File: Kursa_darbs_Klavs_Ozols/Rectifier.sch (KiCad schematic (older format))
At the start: 75 parts, among them U10 TL074, U11 TL074, U12 TL074

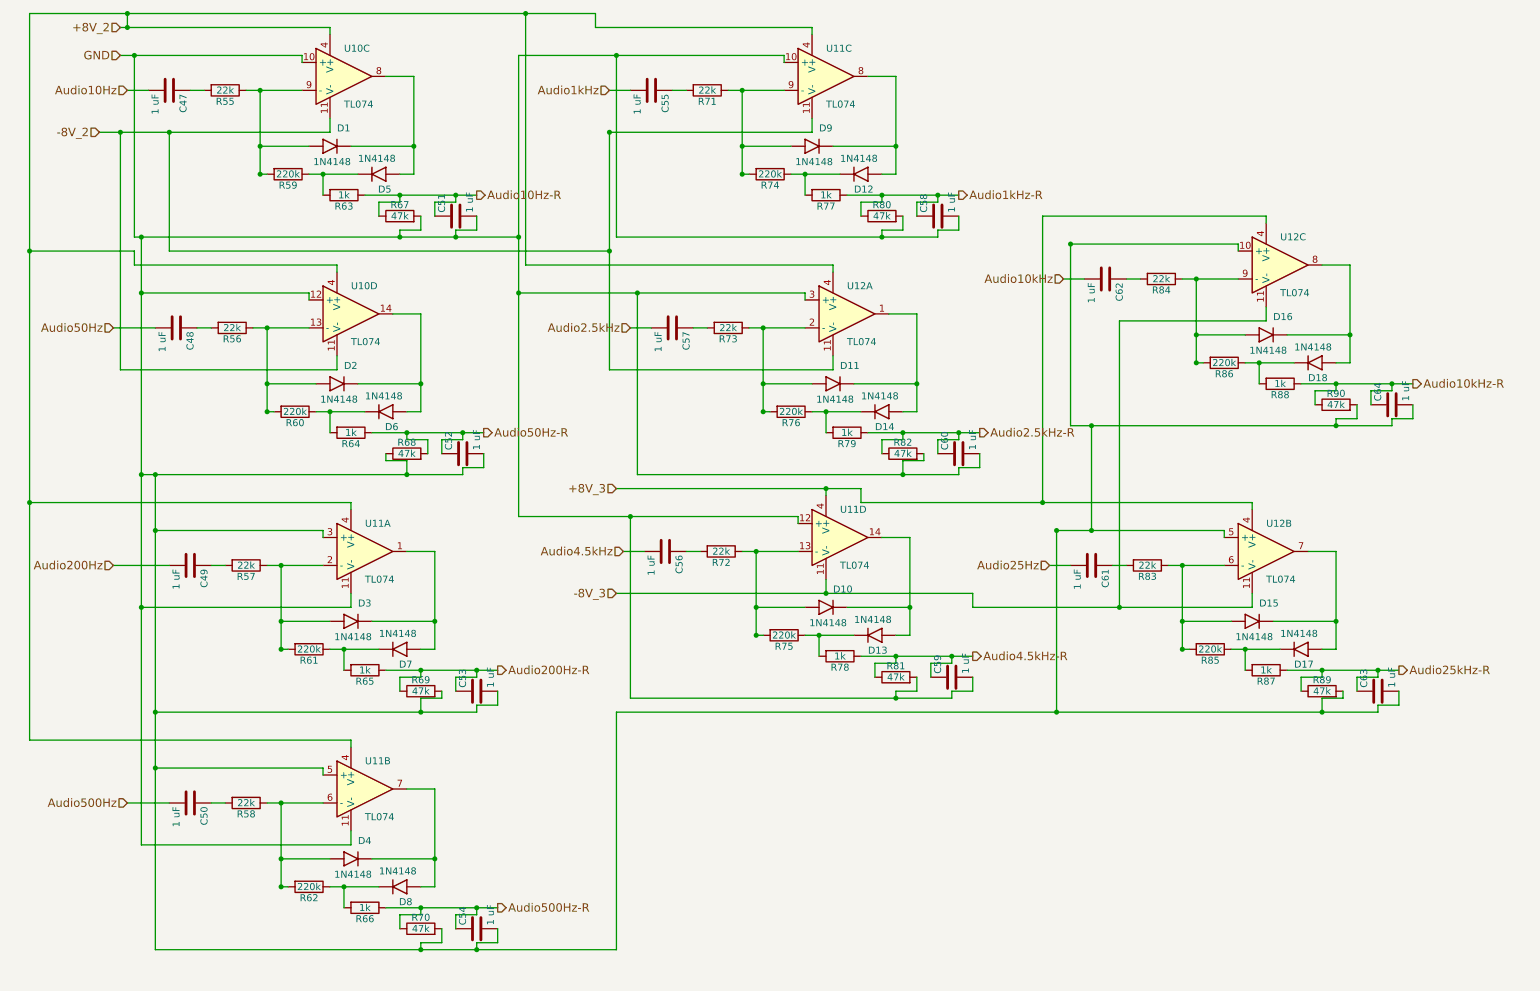
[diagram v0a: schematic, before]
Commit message: Kursa darba plates 4. iteraacija
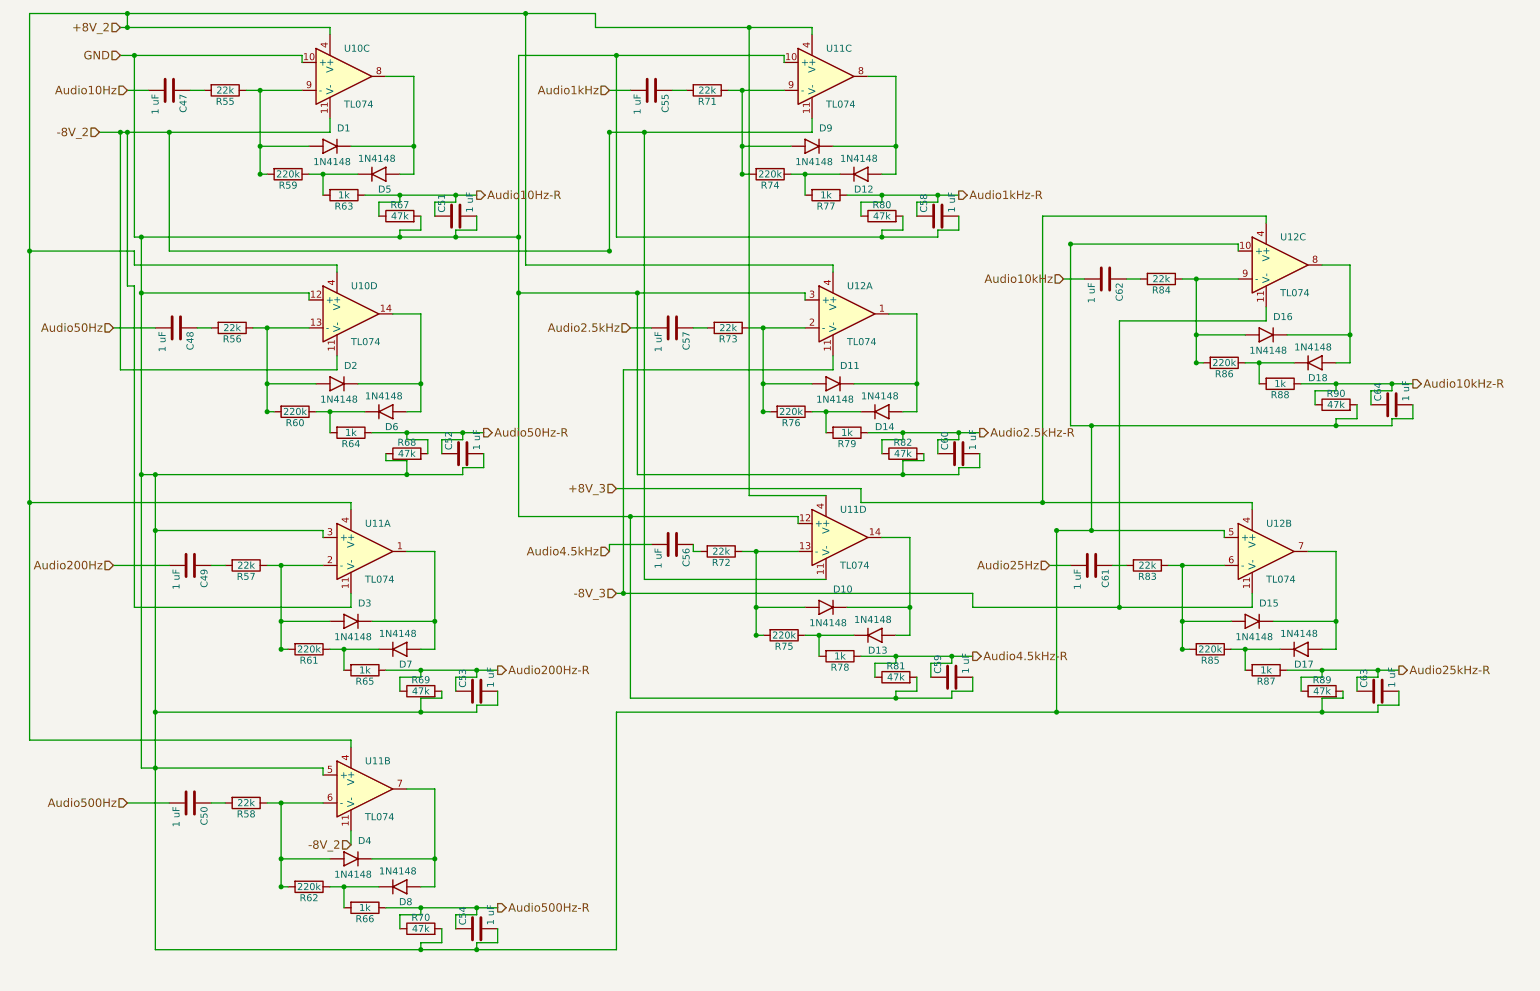
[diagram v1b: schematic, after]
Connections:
- net +8V_2: now also U11.4 (V+)
- net +8V_3: no longer U11.4 (V+)
- net -8V_2: now also U11.11 (V-), U11.11 (V-), U11.11 (V-); no longer U12.11 (V-)
- net -8V_3: now also U12.11 (V-); no longer U11.11 (V-)
- net GND: no longer U11.11 (V-), U11.11 (V-)
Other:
- moved on the sheet: C56
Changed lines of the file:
@@
 	1    0    0    -1
 $EndComp
-Text HLabel 4800 4400 0    60   Input ~ 0
+Text HLabel 4700 4400 0    60   Input ~ 0
 Audio4.5kHz
 $Comp
 L C C56
 U 1 1 5B02E4FB
-P 5100 4400
-F 0 "C56" H 5125 4500 50  0000 L CNN
-F 1 "1 uF" H 5125 4300 50  0000 L CNN
-F 2 "Capacitors_THT:C_Axial_L5.1mm_D3.1mm_P10.00mm_Horizontal" H 5138 4250 50  0001 C CNN
-F 3 "https://eu.mouser.com/datasheet/2/212/KEM_C1046_AXIAL_MOLDED_X7R-1145195.pdf" H 5100 4400 50  0001 C CNN
-	1    5100 4400
+P 5150 4350
+F 0 "C56" H 5175 4450 50  0000 L CNN
+F 1 "1 uF" H 5175 4250 50  0000 L CNN
+F 2 "Capacitors_THT:C_Axial_L5.1mm_D3.1mm_P10.00mm_Horizontal" H 5188 4200 50  0001 C CNN
+F 3 "https://eu.mouser.com/datasheet/2/212/KEM_C1046_AXIAL_MOLDED_X7R-1145195.pdf" H 5150 4350 50  0001 C CNN
+	1    5150 4350
 	0    1    1    0
 $EndComp
@@
 Connection ~ 3250 3850
 Connection ~ 1350 3850
-Wire Wire Line
-	1350 2150 1350 6500
 Connection ~ 3650 3550
 Wire Wire Line
@@
 Wire Wire Line
 	550  4050 2850 4050
-Wire Wire Line
-	1350 4800 2850 4800
 Wire Wire Line
 	2850 4800 2850 4700
@@
 	550  5750 2850 5750
 Wire Wire Line
-	1350 6500 2850 6500
-Wire Wire Line
 	2850 6500 2850 6400
 Wire Wire Line
@@
 	4100 2350 6300 2350
 Wire Wire Line
-	4700 3100 6300 3100
-Wire Wire Line
 	6300 3100 6300 3000
 Wire Wire Line
@@
 Connection ~ 7200 3550
 Wire Wire Line
-	4950 4400 4800 4400
-Wire Wire Line
-	5350 4400 5250 4400
-Wire Wire Line
 	6050 4400 5650 4400
 Wire Wire Line
@@
 Connection ~ 6750 5150
 Wire Wire Line
-	6250 4000 6250 3950
-Wire Wire Line
 	4750 3950 6500 3950
-Wire Wire Line
-	4750 4700 7300 4700
-Wire Wire Line
-	6250 4700 6250 4600
 Wire Wire Line
 	6050 4150 6050 4200
@@
 	2650 4250 1450 4250
 Wire Wire Line
-	2650 5950 1450 5950
+	1350 5950 2650 5950
 Connection ~ 4050 2150
 Connection ~ 4050 2550
@@
 Connection ~ 550  2250
 Connection ~ 550  4050
-Connection ~ 1350 4800
 Connection ~ 1250 550
 Wire Wire Line
@@
 Wire Wire Line
 	1550 2250 4700 2250
-Wire Wire Line
-	4700 1400 4700 3100
 Connection ~ 4700 1400
 Connection ~ 1550 1400
@@
 Wire Wire Line
 	6500 3950 6500 4050
-Connection ~ 6250 3950
 Wire Wire Line
 	7300 4700 7300 4800
-Connection ~ 6250 4700
 Wire Wire Line
 	7800 2000 7800 4050
@@
 Wire Wire Line
 	3750 7200 3750 7250
+Wire Wire Line
+	2850 4800 1300 4800
+Wire Wire Line
+	1300 4800 1300 2500
+Wire Wire Line
+	1300 2500 1250 2500
+Wire Wire Line
+	1250 2500 1250 1400
+Connection ~ 1250 1400
+Wire Wire Line
+	4700 2250 4700 1400
+Wire Wire Line
+	4800 4700 4800 3100
+Connection ~ 4800 4700
+Wire Wire Line
+	4800 3100 6300 3100
+Wire Wire Line
+	4750 4700 7300 4700
+Wire Wire Line
+	6250 4600 4950 4600
+Wire Wire Line
+	4950 4600 4950 1400
+Connection ~ 4950 1400
+Wire Wire Line
+	6250 4000 5700 4000
+Wire Wire Line
+	5700 4000 5700 650
+Connection ~ 5700 650
+Wire Wire Line
+	1350 2150 1350 5950
+Text HLabel 2850 6500 0    60   Input ~ 0
+-8V_2
+Wire Wire Line
+	5300 4400 5300 4350
+Wire Wire Line
+	5350 4400 5300 4400
+Wire Wire Line
+	5000 4350 4700 4350
+Wire Wire Line
+	4700 4350 4700 4400
 $EndSCHEMATC

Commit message: Shiii ir 5. iteraacija manai platei - layouts
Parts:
- removed D10, D11, D12, D13, D14, D15, D16, D17, D18, D2, D3, D4, D6, D7, D8, D9: 1N4148, 1N4148:DO35-3, symbol 1N4148
- added D10, D11, D12, D13, D14, D15, D16, D17, D18, D2, D3, D4, D6, D7, D8, D9: 1N4148, 1N4148:DIOMELF3515N, symbol 1N4148-RESCUE-Kursa_darbs_Klavs_Ozols
- C47, C48, C49, C50, C51, C52, C53, C54, C55, C56, C57, C58, C59, C60, C61, C62, C63, C64: footprint Capacitors_THT:C_Axial_L5.1mm_D3.1mm_P10.00mm_Horizontal -> Capacitors_SMD:C_0805_HandSoldering
- D1, D5: footprint 1N4148:DO35-3 -> 1N4148:DIOMELF3515N; symbol 1N4148 -> 1N4148-RESCUE-Kursa_darbs_Klavs_Ozols
- R55, R56, R57, R58, R59, R60, R61, R62, R63, R64, R65, R66, R67, R68, R69, R70, R71, R72, R73, R74, R75, R76, R77, R78, R79, R80, R81, R82, R83, R84, R85, R86, R87, R88, R89, R90: footprint Resistors_THT:R_Axial_DIN0309_L9.0mm_D3.2mm_P5.08mm_Vertical -> Resistors_SMD:R_0805_HandSoldering
- U10, U11, U12: footprint TL074:DIL14 -> TL074:SO14
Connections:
- net Audio25Hz is gone; now on net Audio10kHz: C61.2
- net +8V_2: no longer U11.4 (V+)
- net +8V_3: now also U11.4 (V+)
- net -8V_2: now also U12.11 (V-); no longer U11.11 (V-)
- net -8V_3: now also U11.11 (V-); no longer U12.11 (V-)
- net Audio10kHz: no longer C62.2
- net Audio10kHz-R: now also C63.1, R87.1, R89.1; no longer C64.1, R88.1, R90.1
- net Audio2.5kHz: now also C56.2; no longer C57.2
- net Audio2.5kHz-R: now also C59.1, R78.1, R81.1; no longer C60.1, R79.1, R82.1
- net Audio200Hz: now also C50.2; no longer C49.2
- net Audio200Hz-R: now also C54.1, R66.1, R70.1; no longer C53.1, R65.1, R69.1
- net Audio25kHz-R: now also C64.1, R88.1, R90.1; no longer C63.1, R87.1, R89.1
- net Audio4.5kHz: now also C57.2; no longer C56.2
- net Audio4.5kHz-R: now also C60.1, R79.1, R82.1; no longer C59.1, R78.1, R81.1
- net Audio500Hz: now also C49.2; no longer C50.2
- net Audio500Hz-R: now also C53.1, R65.1, R69.1; no longer C54.1, R66.1, R70.1
- net Audio50Hz-R: now also R68.1; no longer R68.2
- net GND: now also R68.2; no longer R68.1
- net at R56.1, R60.2, U10.13 (-): now also D2.A
- net at U10.14: now also D2.C, D3.A
- net at R60.1, R64.2: now also D3.C
- net at U11.1: now also D4.C, D7.A
- net at R57.1, R61.2, U11.2 (-): now also D4.A
- net at R61.1, R65.2: now also D7.C
- net at R58.1, R62.2, U11.6 (-): now also D6.A
- net at U11.7: now also D6.C, D8.A
- net at R62.1, R66.2: now also D8.C
- net at R71.1, R74.2, U11.9 (-): now also D9.A
- net at U11.8: now also D12.A, D9.C
- net at R74.1, R77.2: now also D12.C
- net at R73.1, R76.2, U12.2 (-): now also D11.A
- net at U12.1: now also D11.C, D14.A
- net at R76.1, R79.2: now also D14.C
- net at R72.1, R75.2, U11.13 (-): now also D10.A
- net at U11.14: now also D10.C, D13.A
- net at R75.1, R78.2: now also D13.C
- net at R84.1, R86.2, U12.9 (-): now also D16.A
- net at U12.8: now also D16.C, D18.A
- net at R86.1, R88.2: now also D18.C
- net at R83.1, R85.2, U12.6 (-): now also D15.A
- net at U12.7: now also D15.C, D17.A
- net at R85.1, R87.2: now also D17.C
- new net Audio25kHz: C62.2
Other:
- moved on the sheet: C51, R67
